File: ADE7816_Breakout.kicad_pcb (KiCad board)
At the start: 2 copper layers, 66 x 76.2 mm, 56 parts, among them J1 AudioJack3, J2 AudioJack3, J3 AudioJack3, J4 AudioJack3, J5 AudioJack3, J6 AudioJack3, J7 Barrel_Jack_Switch, J8 Conn_01x10, U1 ADE7816ACPZ, Y1 16.384MHz

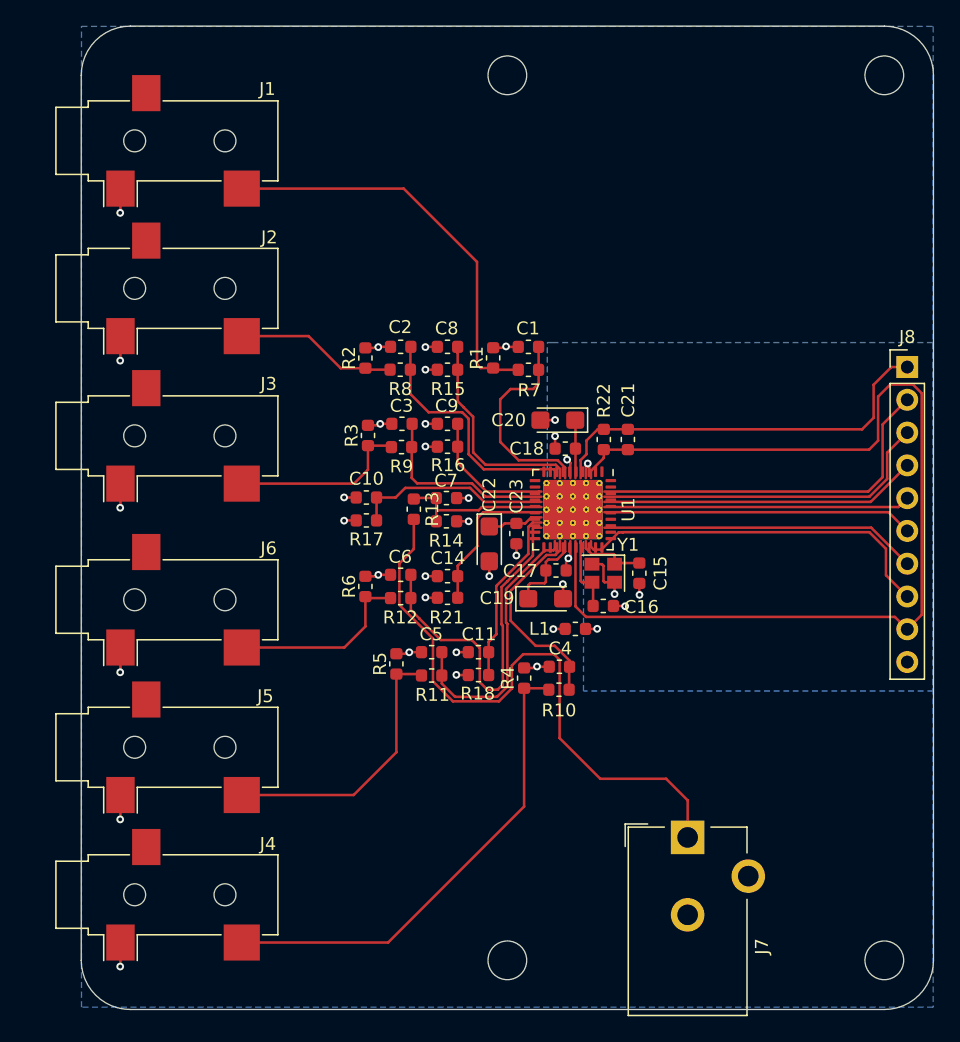
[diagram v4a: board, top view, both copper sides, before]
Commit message: - Updated U1 to use QFN40 6x6mm 0.5 pitch on both schematic and PCB and updated the layout to accomidate this. - moved all footprint files to the modules directory - created modified footprint for the barrel jack to accomidate flat pins and use slots instead of round holes. - added top ground plane and via stitching
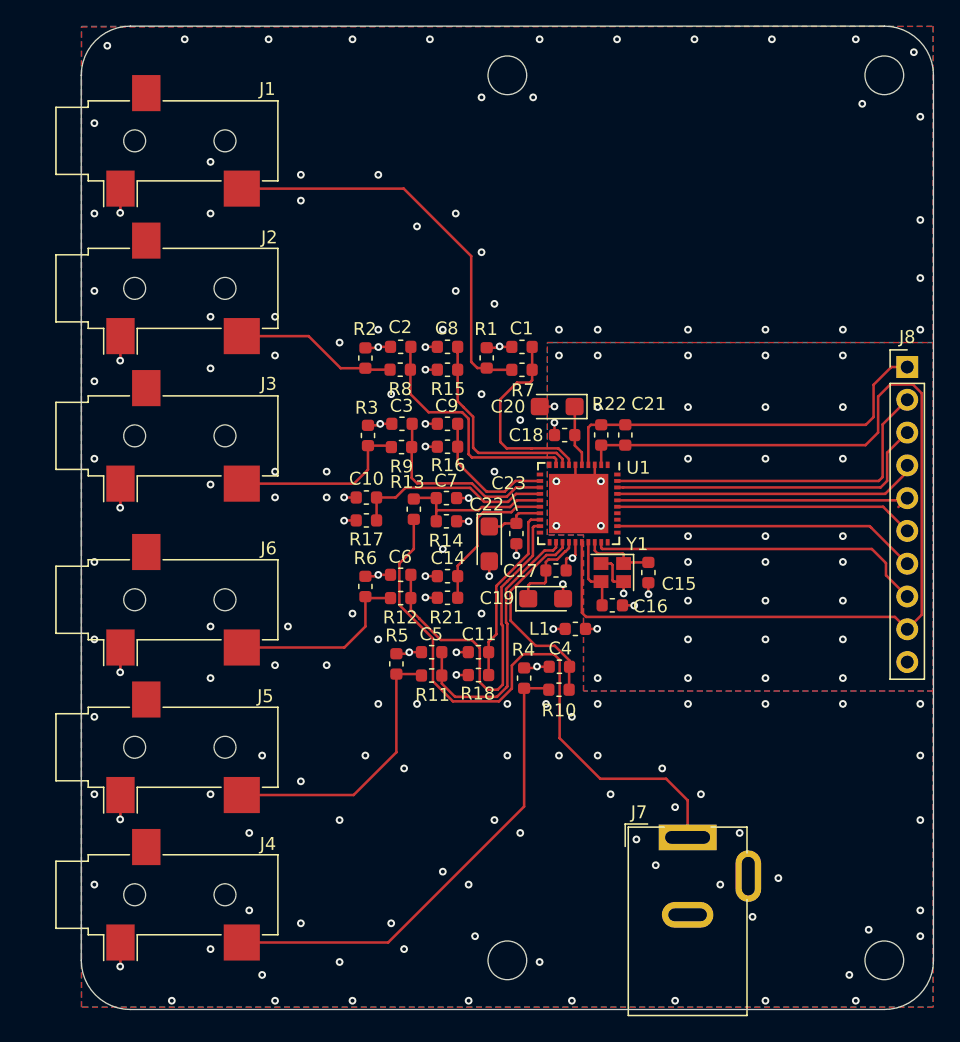
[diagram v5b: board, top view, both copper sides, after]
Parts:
- J1, J2, J3, J4, J5, J6: footprint misc:Jack_3.5mm_CUI_SJ-3523-SMT_Horizontal -> modules:Jack_3.5mm_CUI_SJ-3523-SMT_Horizontal
- J7: footprint Connectors:Barrel_Jack_CUI_PJ-102AH -> modules:Barrel_Jack_CUI_PJ-002A
- U1: footprint Package_DFN_QFN:QFN-40-1EP_6x6mm_P0.5mm_EP4.6x4.6mm_ThermalVias -> Housings_DFN_QFN:QFN-40-1EP_6x6mm_Pitch0.5mm
- moved C18 1.05 mm to (131.4, 62.2)
- moved C20 1.05 mm to (130.9, 60.0)
- moved C16 0.70 mm to (135.1, 75.4)
- moved Y1 0.70 mm to (135.1, 72.8)
- moved C15 0.70 mm to (137.9, 72.8)
- moved U1 0.65 mm to (132.5, 67.5)
- moved C1 0.50 mm to (128.1, 55.3)
- moved R1 0.50 mm to (125.4, 56.2)
- moved R7 0.50 mm to (128.1, 57.1)
- moved C21 0.40 mm to (136.1, 62.2)
- moved R22 0.40 mm to (134.3, 62.2)
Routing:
- net GNDD: track 11.5 -> 26.6 mm, vias 8 -> 38
- net /meter_module/~IRQ0: track 28.9 -> 26.3 mm
- net +3V3: track 81.9 -> 80.2 mm
- net /meter_module/~CS: track 28.8 -> 27.5 mm
- net /meter_module/MOSI: track 26.7 -> 25.5 mm
- net /meter_module/MISO: track 24.6 -> 23.7 mm
- net /meter_module/~IRQ1: track 24.6 -> 23.7 mm
- net IAP: track 16.3 -> 15.3 mm
- net /meter_module/HSCLK: track 24.1 -> 23.2 mm
- net /meter_module/~RESET: track 31.8 -> 31.0 mm
- net IAN: track 17.1 -> 16.5 mm
- net GNDA: track 41.0 -> 41.3 mm, vias 29 -> 154
- added copper zone on F.Cu, net GNDA
- added copper zone on F.Cu, net GNDD

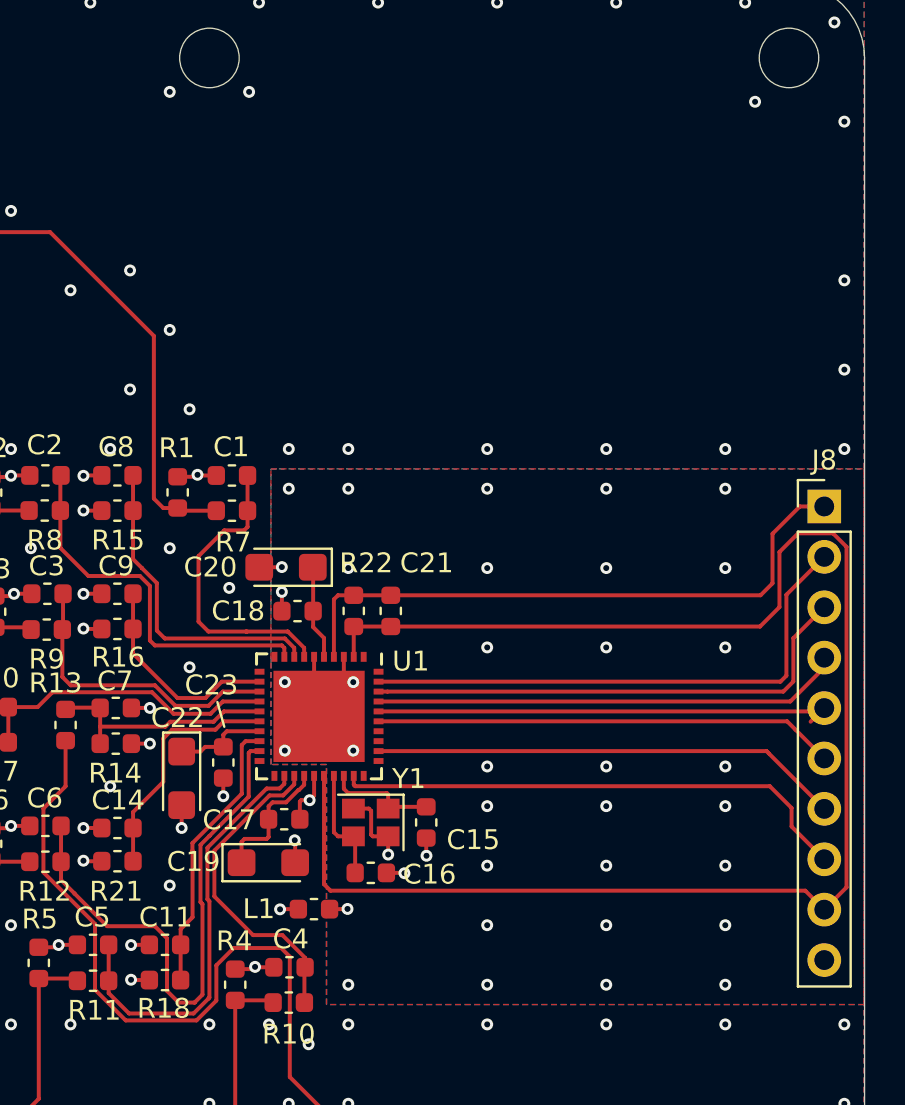
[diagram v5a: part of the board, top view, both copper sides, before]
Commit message: Add silk screen details
Signed-off-by: Tisham Dhar <whatnickd@gmail.com>
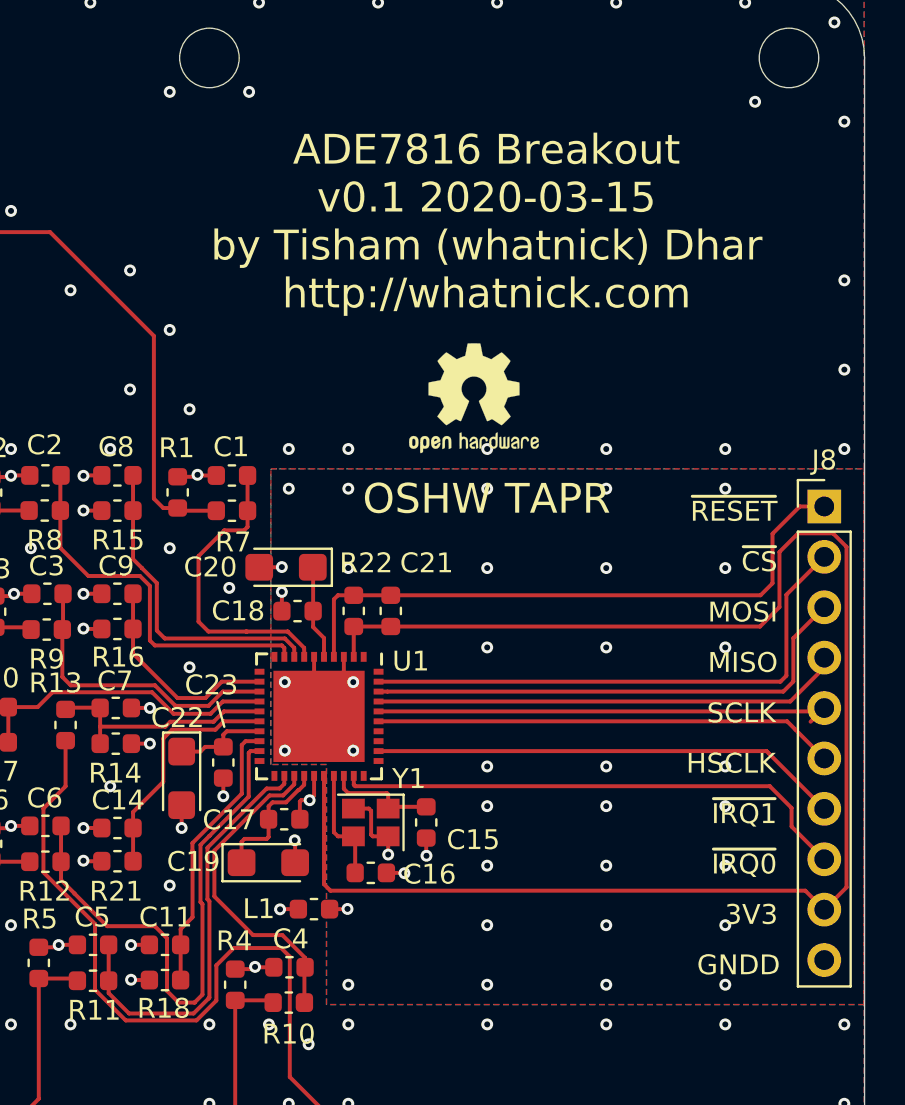
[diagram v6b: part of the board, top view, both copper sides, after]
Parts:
- added LOGO1: OSHW-Logo2_7.3x6mm_SilkScreen, Symbol:OSHW-Logo2_7.3x6mm_SilkScreen, F.Cu at (140.3, 51.4)
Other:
- board text added: "3V3"
- board text added: "ADE7816 Breakout v0.1 2020-03-15 by Tisham (whatnick) Dhar http://whatnick.com"
- board text added: "GNDD"
- board text added: "HSCLK"
- board text added: "MISO"
- board text added: "MOSI"
- board text added: "OSHW TAPR"
- board text added: "SCLK"
- board text added: "~CS"
- board text added: "~IRQ0"
- board text added: "~IRQ1"
- board text added: "~RESET"

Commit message: Label nets for currents
Signed-off-by: Tisham Dhar <whatnickd@gmail.com>
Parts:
- LOGO1: value OSHW-Logo2_7.3x6mm_SilkScreen -> Logo_Open_Hardware_Small
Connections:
- net Net-(J1-Pad2) renamed /analog_inputs/IA
- net Net-(J2-Pad2) renamed /analog_inputs/IB
- net Net-(J3-Pad2) renamed /analog_inputs/IC
- net Net-(J4-Pad2) renamed /analog_inputs/ID
- net Net-(J5-Pad2) renamed /analog_inputs/IE
- net Net-(J6-Pad2) renamed /analog_inputs/IF

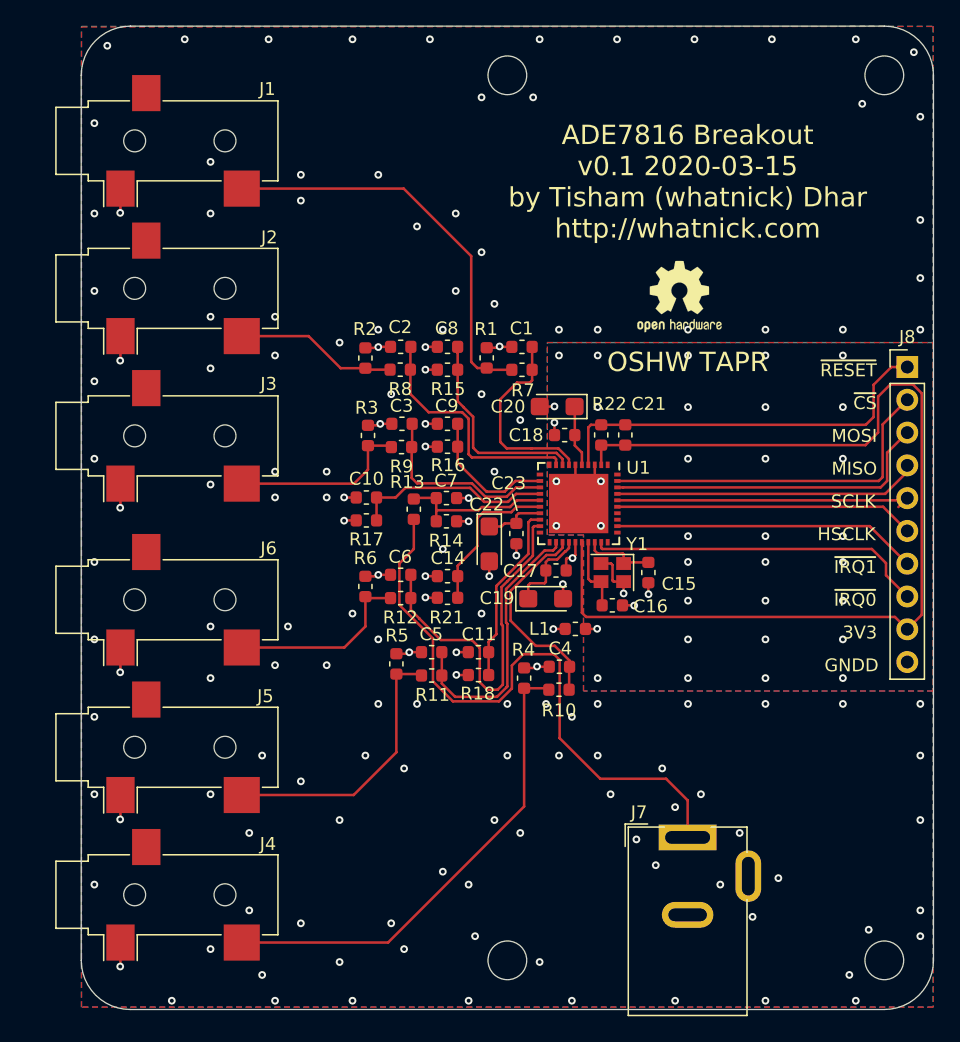
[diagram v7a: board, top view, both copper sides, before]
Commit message: Add more silk screen
Signed-off-by: Tisham Dhar <whatnickd@gmail.com>
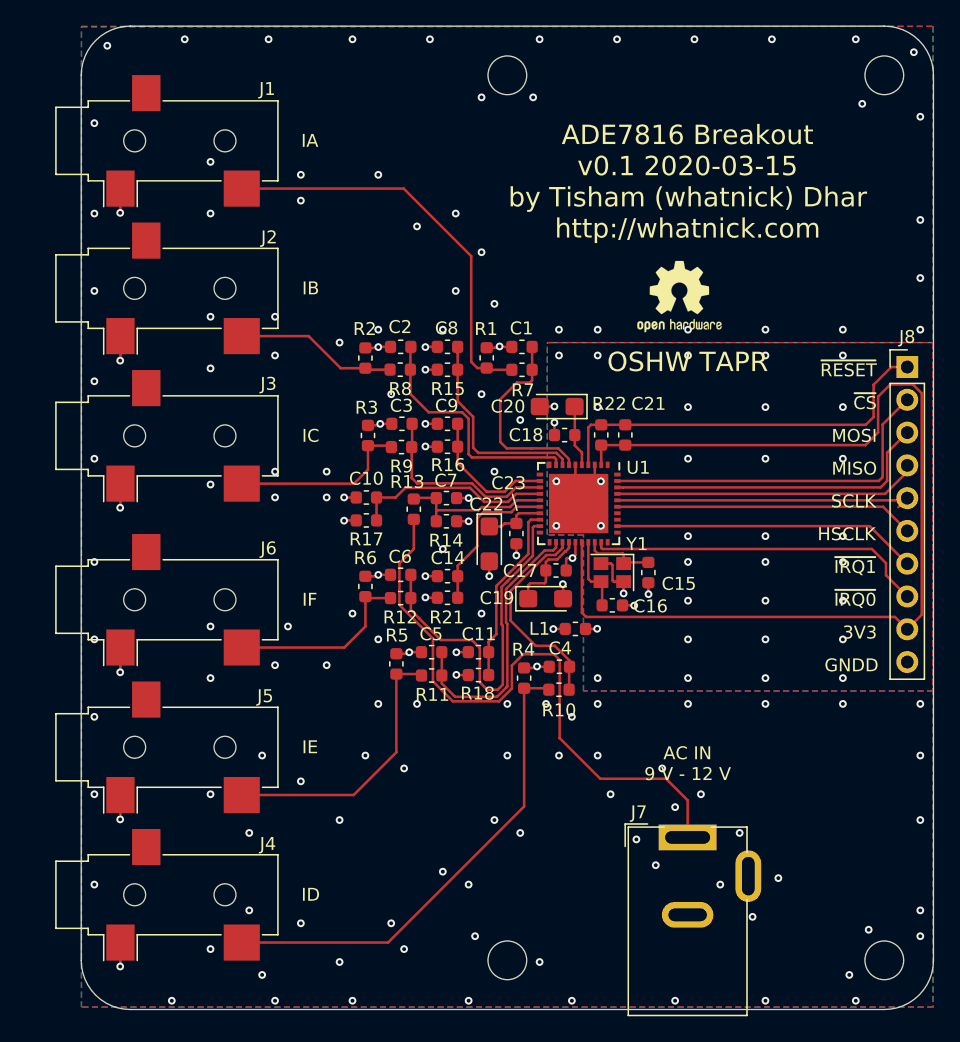
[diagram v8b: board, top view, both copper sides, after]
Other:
- board text added: "AC IN 9 V - 12 V"
- board text added: "IA"
- board text added: "IB"
- board text added: "IC"
- board text added: "ID"
- board text added: "IE"
- board text added: "IF"
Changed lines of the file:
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@@
   (general
     (thickness 1.6)
-    (drawings 33)
+    (drawings 41)
     (tracks 562)
     (zones 0)
@@
     )
   )
+  (dimension 29.21 (width 0.15) (layer Dwgs.User)
+    (gr_text "29.210 mm" (at 141.605 116.235) (layer Dwgs.User)
+      (effects (font (size 1 1) (thickness 0.15)))
+    )
+    (feature1 (pts (xy 156.21 102.87) (xy 156.21 115.521421)))
+    (feature2 (pts (xy 127 102.87) (xy 127 115.521421)))
+    (crossbar (pts (xy 127 114.935) (xy 156.21 114.935)))
+    (arrow1a (pts (xy 156.21 114.935) (xy 155.083496 115.521421)))
+    (arrow1b (pts (xy 156.21 114.935) (xy 155.083496 114.348579)))
+    (arrow2a (pts (xy 127 114.935) (xy 128.126504 115.521421)))
+    (arrow2b (pts (xy 127 114.935) (xy 128.126504 114.348579)))
+  )
+  (gr_text "AC IN\n9 V - 12 V" (at 140.97 87.63) (layer F.SilkS)
+    (effects (font (size 1 1) (thickness 0.15)))
+  )
+  (gr_text ID (at 111.76 97.79) (layer F.SilkS)
+    (effects (font (size 1 1) (thickness 0.15)))
+  )
+  (gr_text IE (at 111.712381 86.36) (layer F.SilkS)
+    (effects (font (size 1 1) (thickness 0.15)))
+  )
+  (gr_text IF (at 111.688571 74.93) (layer F.SilkS)
+    (effects (font (size 1 1) (thickness 0.15)))
+  )
+  (gr_text IC (at 111.76 62.23) (layer F.SilkS)
+    (effects (font (size 1 1) (thickness 0.15)))
+  )
+  (gr_text IB (at 111.76 50.8) (layer F.SilkS)
+    (effects (font (size 1 1) (thickness 0.15)))
+  )
+  (gr_text IA (at 111.688571 39.37) (layer F.SilkS)
+    (effects (font (size 1 1) (thickness 0.15)))
+  )
   (gr_text GNDD (at 153.67 80.01) (layer B.SilkS)
